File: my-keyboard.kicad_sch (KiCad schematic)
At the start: 156 parts, among them J1 AVR-ISP-6, SW1 SW_Push, U1 ATmega32U4-AU, Y1 16MHz

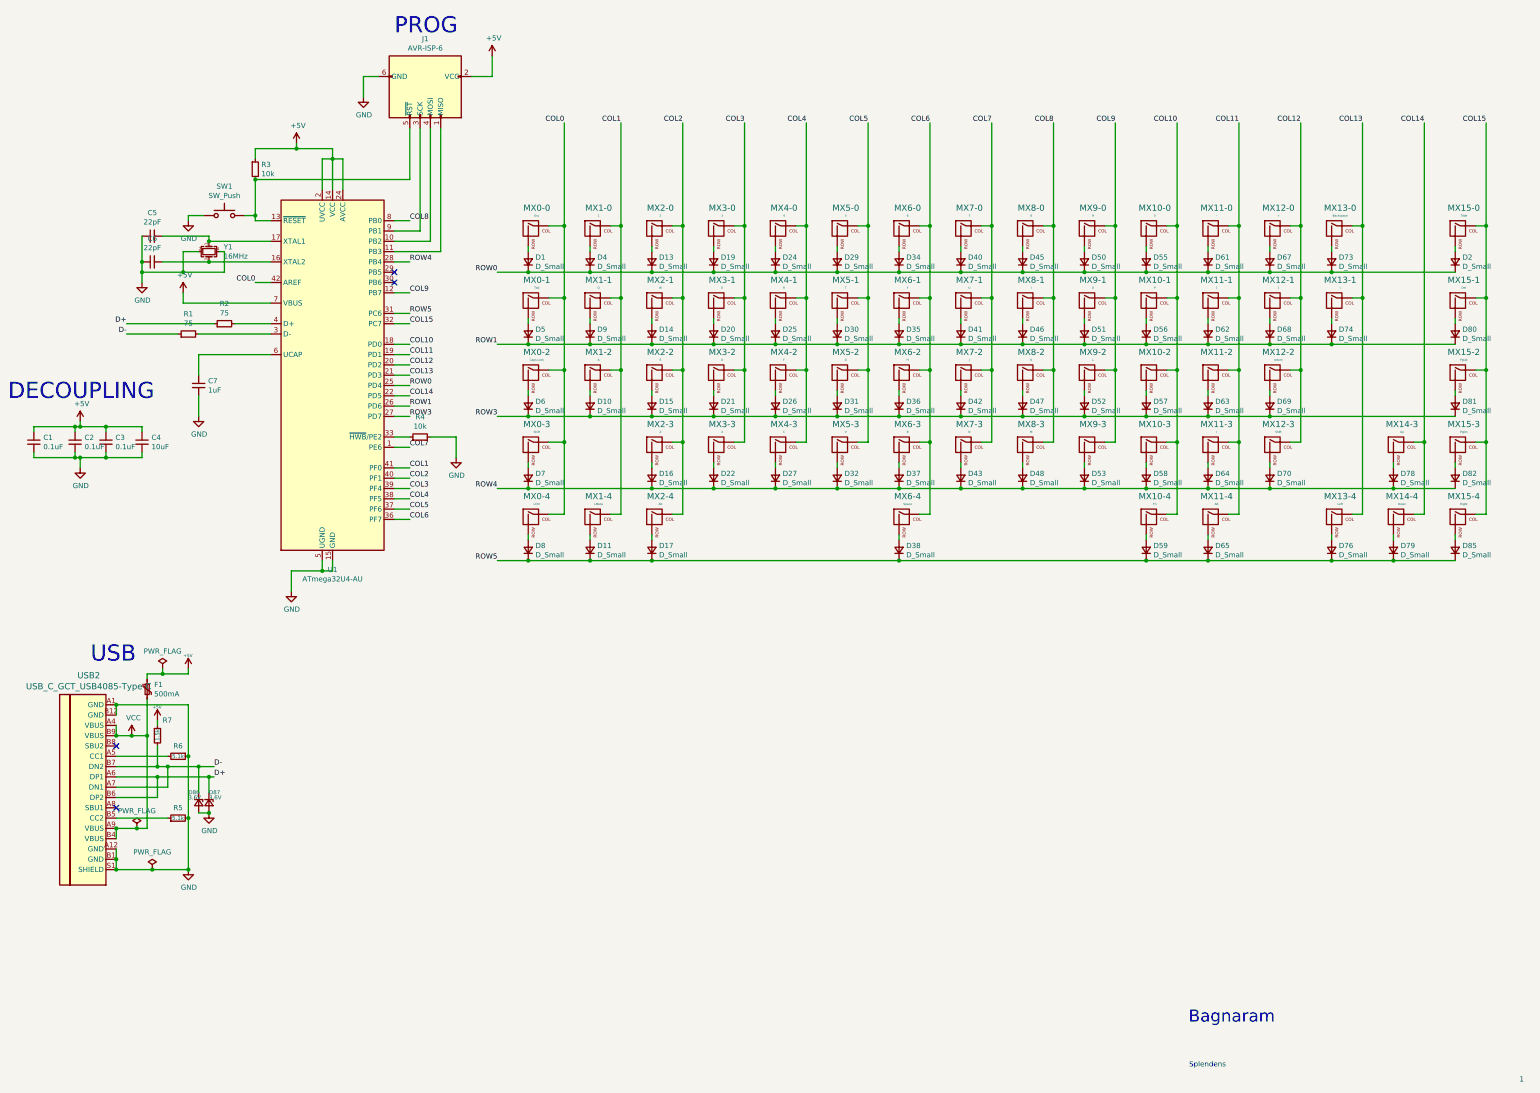
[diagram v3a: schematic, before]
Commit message: different usb footprint
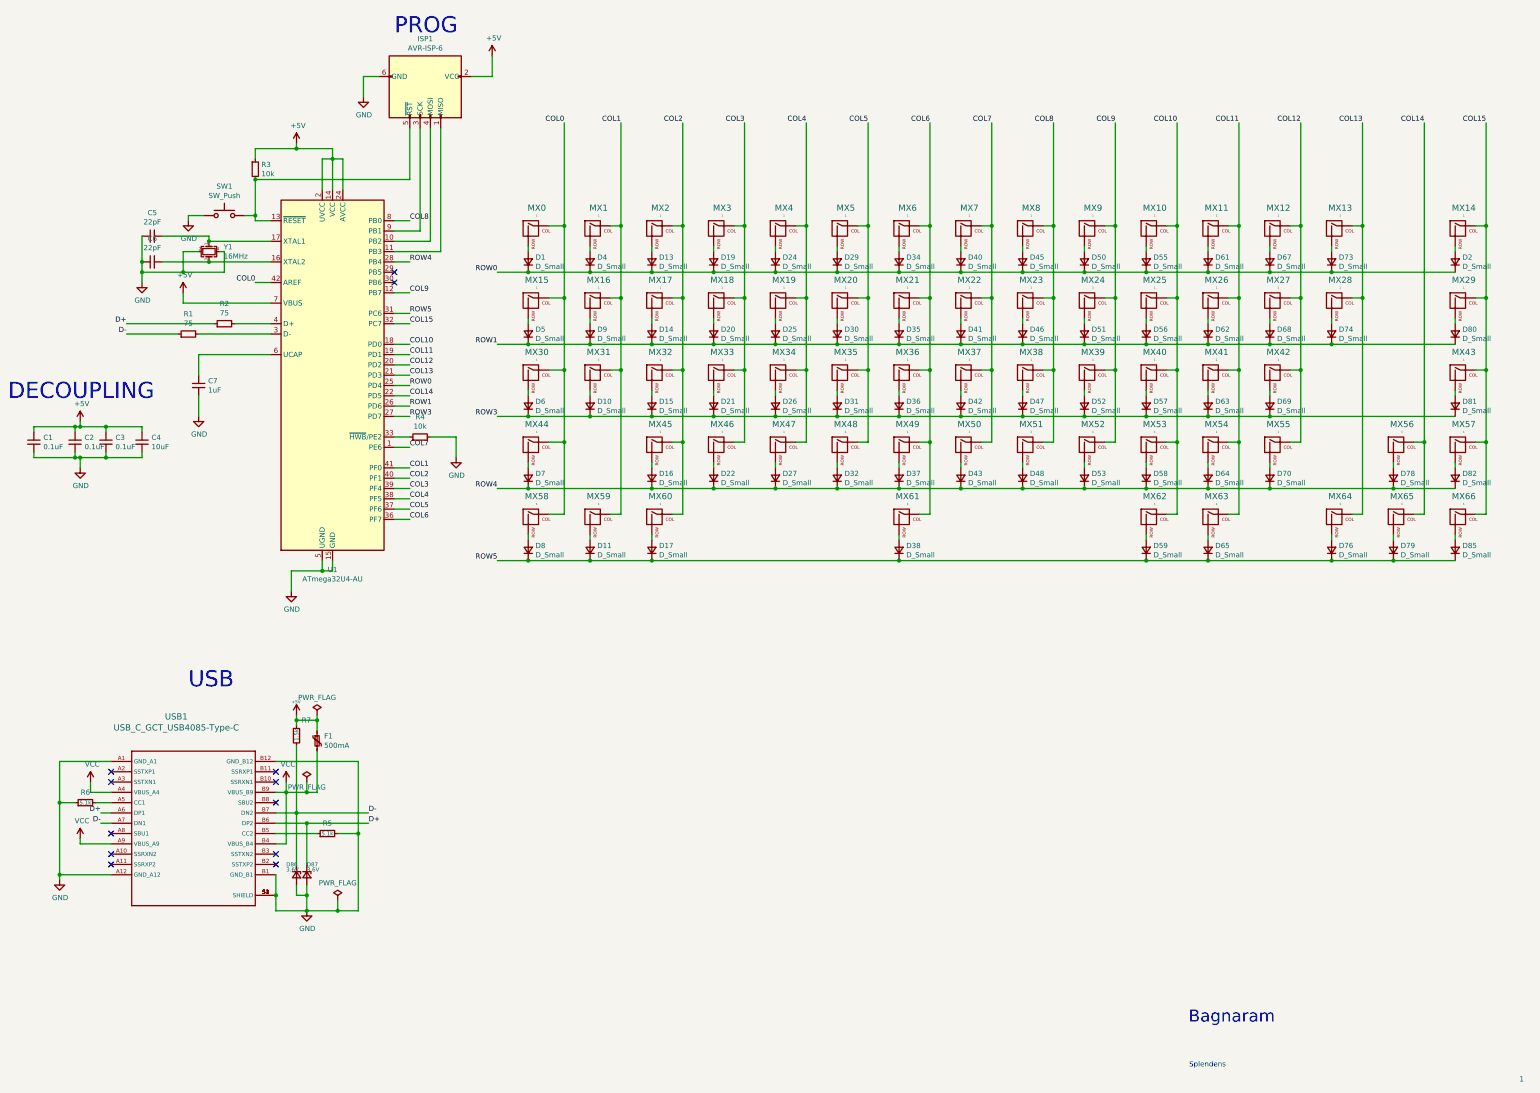
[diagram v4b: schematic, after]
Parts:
- C1, C2, C3: SKU (none) -> CC0805JPX7R8BB104
- C4: SKU (none) -> CGA4J1X7S1E106K125AC
- C5, C6: SKU (none) -> C0805X220K3GACAUTO
- C7: SKU (none) -> C0805C105M8RACAUTO
- D1, D10, D11, D13, D14, D15, D16, D17, D19, D2, D20, D21, D22, D24, D25, D26, D27, D29, D30, D31, D32, D34, D35, D36, D37, D38, D4, D40, D41, D42, D43, D45, D46, D47, D48, D5, D50, D51, D52, D53, D55, D56, D57, D58, D59, D6, D61, D62, D63, D64, D65, D67, D68, D69, D7, D70, D73, D74, D76, D78, D79, D8, D80, D81, D82, D85, D9: SKU (none) -> 1N4148W-E3-08
- D86, D87: SKU (none) -> MMSZ4685T1G
- F1: SKU (none) -> MF-R050
- ISP1: renamed from J1; SKU (none) -> 68602-406HLF
- MX0: renamed from MX0-0; value Esc -> 1; SKU (none) -> PCB Mount Gateron Switches (5 Legs) Brown
- MX1: renamed from MX1-0; SKU (none) -> PCB Mount Gateron Switches (5 Legs) Brown
- MX10: renamed from MX10-0; value 0 -> 1; SKU (none) -> PCB Mount Gateron Switches (5 Legs) Brown
- MX11: renamed from MX11-0; value - -> 1; SKU (none) -> PCB Mount Gateron Switches (5 Legs) Brown
- MX12: renamed from MX12-0; value = -> 1; SKU (none) -> PCB Mount Gateron Switches (5 Legs) Brown
- MX13: renamed from MX13-0; value Backspace -> 1; SKU (none) -> PCB Mount Gateron Switches (5 Legs) Brown
- MX14: renamed from MX15-0; value Tilde -> 1; SKU (none) -> PCB Mount Gateron Switches (5 Legs) Brown
- MX15: renamed from MX0-1; value Tab -> 1; SKU (none) -> PCB Mount Gateron Switches (5 Legs) Brown
- MX16: renamed from MX1-1; value Q -> 1; SKU (none) -> PCB Mount Gateron Switches (5 Legs) Brown
- MX17: renamed from MX2-1; value W -> 1; SKU (none) -> PCB Mount Gateron Switches (5 Legs) Brown
- MX18: renamed from MX3-1; value E -> 1; SKU (none) -> PCB Mount Gateron Switches (5 Legs) Brown
- MX19: renamed from MX4-1; value R -> 1; SKU (none) -> PCB Mount Gateron Switches (5 Legs) Brown
- MX2: renamed from MX2-0; value 2 -> 1; SKU (none) -> PCB Mount Gateron Switches (5 Legs) Brown
- MX20: renamed from MX5-1; value T -> 1; SKU (none) -> PCB Mount Gateron Switches (5 Legs) Brown
- MX21: renamed from MX6-1; value Y -> 1; SKU (none) -> PCB Mount Gateron Switches (5 Legs) Brown
- MX22: renamed from MX7-1; value U -> 1; SKU (none) -> PCB Mount Gateron Switches (5 Legs) Brown
- MX23: renamed from MX8-1; value I -> 1; SKU (none) -> PCB Mount Gateron Switches (5 Legs) Brown
- MX24: renamed from MX9-1; value O -> 1; SKU (none) -> PCB Mount Gateron Switches (5 Legs) Brown
- MX25: renamed from MX10-1; value P -> 1; SKU (none) -> PCB Mount Gateron Switches (5 Legs) Brown
- MX26: renamed from MX11-1; value [ -> 1; SKU (none) -> PCB Mount Gateron Switches (5 Legs) Brown
- MX27: renamed from MX12-1; value ] -> 1; SKU (none) -> PCB Mount Gateron Switches (5 Legs) Brown
- MX28: renamed from MX13-1; value \ -> 1; SKU (none) -> PCB Mount Gateron Switches (5 Legs) Brown
- MX29: renamed from MX15-1; value Del -> 1; SKU (none) -> PCB Mount Gateron Switches (5 Legs) Brown
- MX3: renamed from MX3-0; value 3 -> 1; SKU (none) -> PCB Mount Gateron Switches (5 Legs) Brown
- MX30: renamed from MX0-2; value Caps Lock -> 1; SKU (none) -> PCB Mount Gateron Switches (5 Legs) Brown
- MX31: renamed from MX1-2; value A -> 1; SKU (none) -> PCB Mount Gateron Switches (5 Legs) Brown
- MX32: renamed from MX2-2; value S -> 1; SKU (none) -> PCB Mount Gateron Switches (5 Legs) Brown
- MX33: renamed from MX3-2; value D -> 1; SKU (none) -> PCB Mount Gateron Switches (5 Legs) Brown
- MX34: renamed from MX4-2; value F -> 1; SKU (none) -> PCB Mount Gateron Switches (5 Legs) Brown
- MX35: renamed from MX5-2; value G -> 1; SKU (none) -> PCB Mount Gateron Switches (5 Legs) Brown
- MX36: renamed from MX6-2; value H -> 1; SKU (none) -> PCB Mount Gateron Switches (5 Legs) Brown
- MX37: renamed from MX7-2; value J -> 1; SKU (none) -> PCB Mount Gateron Switches (5 Legs) Brown
- MX38: renamed from MX8-2; value K -> 1; SKU (none) -> PCB Mount Gateron Switches (5 Legs) Brown
- MX39: renamed from MX9-2; value L -> 1; SKU (none) -> PCB Mount Gateron Switches (5 Legs) Brown
- MX4: renamed from MX4-0; value 4 -> 1; SKU (none) -> PCB Mount Gateron Switches (5 Legs) Brown
- MX40: renamed from MX10-2; value ; -> 1; SKU (none) -> PCB Mount Gateron Switches (5 Legs) Brown
- MX41: renamed from MX11-2; value ' -> 1; SKU (none) -> PCB Mount Gateron Switches (5 Legs) Brown
- MX42: renamed from MX12-2; value return -> 1; SKU (none) -> PCB Mount Gateron Switches (5 Legs) Brown
- MX43: renamed from MX15-2; value PgUp -> 1; SKU (none) -> PCB Mount Gateron Switches (5 Legs) Brown
- MX44: renamed from MX0-3; value Shift -> 1; SKU (none) -> PCB Mount Gateron Switches (5 Legs) Brown
- MX45: renamed from MX2-3; value Z -> 1; SKU (none) -> PCB Mount Gateron Switches (5 Legs) Brown
- MX46: renamed from MX3-3; value X -> 1; SKU (none) -> PCB Mount Gateron Switches (5 Legs) Brown
- MX47: renamed from MX4-3; value C -> 1; SKU (none) -> PCB Mount Gateron Switches (5 Legs) Brown
- MX48: renamed from MX5-3; value V -> 1; SKU (none) -> PCB Mount Gateron Switches (5 Legs) Brown
- MX49: renamed from MX6-3; value B -> 1; SKU (none) -> PCB Mount Gateron Switches (5 Legs) Brown
- MX5: renamed from MX5-0; value 5 -> 1; SKU (none) -> PCB Mount Gateron Switches (5 Legs) Brown
- MX50: renamed from MX7-3; value N -> 1; SKU (none) -> PCB Mount Gateron Switches (5 Legs) Brown
- MX51: renamed from MX8-3; value M -> 1; SKU (none) -> PCB Mount Gateron Switches (5 Legs) Brown
- MX52: renamed from MX9-3; value , -> 1; SKU (none) -> PCB Mount Gateron Switches (5 Legs) Brown
- MX53: renamed from MX10-3; value . -> 1; SKU (none) -> PCB Mount Gateron Switches (5 Legs) Brown
- MX54: renamed from MX11-3; value / -> 1; SKU (none) -> PCB Mount Gateron Switches (5 Legs) Brown
- MX55: renamed from MX12-3; value Shift -> 1; SKU (none) -> PCB Mount Gateron Switches (5 Legs) Brown
- MX56: renamed from MX14-3; value Up -> 1; SKU (none) -> PCB Mount Gateron Switches (5 Legs) Brown
- MX57: renamed from MX15-3; value PgDn -> 1; SKU (none) -> PCB Mount Gateron Switches (5 Legs) Brown
- MX58: renamed from MX0-4; value LCtrl -> 1; SKU (none) -> PCB Mount Gateron Switches (5 Legs) Brown
- MX59: renamed from MX1-4; value LMeta -> 1; SKU (none) -> PCB Mount Gateron Switches (5 Legs) Brown
- MX6: renamed from MX6-0; value 6 -> 1; SKU (none) -> PCB Mount Gateron Switches (5 Legs) Brown
- MX60: renamed from MX2-4; value Alt -> 1; SKU (none) -> PCB Mount Gateron Switches (5 Legs) Brown
- MX61: renamed from MX6-4; value Space -> 1; SKU (none) -> PCB Mount Gateron Switches (5 Legs) Brown
- MX62: renamed from MX10-4; value Fn -> 1; SKU (none) -> PCB Mount Gateron Switches (5 Legs) Brown
- MX63: renamed from MX11-4; value Alt -> 1; SKU (none) -> PCB Mount Gateron Switches (5 Legs) Brown
- MX64: renamed from MX13-4; value Left -> 1; SKU (none) -> PCB Mount Gateron Switches (5 Legs) Brown
- MX65: renamed from MX14-4; value Down -> 1; SKU (none) -> PCB Mount Gateron Switches (5 Legs) Brown
- MX66: renamed from MX15-4; value Right -> 1; SKU (none) -> PCB Mount Gateron Switches (5 Legs) Brown
- MX7: renamed from MX7-0; value 7 -> 1; SKU (none) -> PCB Mount Gateron Switches (5 Legs) Brown
- MX8: renamed from MX8-0; value 8 -> 1; SKU (none) -> PCB Mount Gateron Switches (5 Legs) Brown
- MX9: renamed from MX9-0; value 9 -> 1; SKU (none) -> PCB Mount Gateron Switches (5 Legs) Brown
- R1, R2: SKU (none) -> GWCR0805-75RFT5
- R3, R4: SKU (none) -> WCR0805-10KFI
- R5, R6: SKU (none) -> CR0805-FX-5101ELF
- R7: SKU (none) -> CR0805-FX-1501ELF
- SW1: footprint Random Keyboard Parts:SKQG-1155865 -> Random Keyboard Parts:SKQGADE010; SKU (none) -> SKQGADE010
- U1: SKU (none) -> ATmega32U4-AU
- USB1: renamed from USB2; symbol discipline-pcb-rescue:USB_C_GCT_USB4085-Type-C -> 10137061-00021LF:10137061-00021LF; SKU (none) -> 10137061-00021LF
- Y1: SKU (none) -> NX3225GA-16.000M-STD-CRG-2
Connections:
- net GND: now also USB1.S2 (SHIELD), USB1.S3 (SHIELD), USB1.S4 (SHIELD)
- no-connect marks 4 -> 12
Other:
- moved on the sheet: D86, D87, F1, R5, R6, R7

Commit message: Generated gerbers
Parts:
- removed USB1: USB_C_GCT_USB4085-Type-C, cftkb:USB_C_GCT_USB4085, symbol 10137061-00021LF:10137061-00021LF
- added USB1: Wurth-632723300011, Type-C:Wurth-632723300011, symbol Type-C:Wurth-632723300011
- C1, C2, C3: value 0.1uF -> 0.1u
- C4: value 10uF -> 10u
- C5, C6: value 22pF -> 22p
- C7: value 1uF -> 1u
- R1, R2: value 75 -> 22
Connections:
- net D+: now also USB1.18 (Dp2), USB1.6 (Dp1)
- net D-: now also USB1.19 (Dn2), USB1.7 (Dn1)
- net GND: now also USB1.1 (GND), USB1.12 (GND), USB1.13 (GND), USB1.24 (GND), USB1.25 (Center_Plate_Pin), USB1.26 (Connector_Legs), USB1.27 (Under-Barrel_Pads)
- net VCC: now also USB1.16 (VBUS), USB1.21 (VBUS), USB1.4 (VBUS), USB1.9 (VBUS)
- net at R5.1: now also USB1.17 (CC2)
- net at R6.2: now also USB1.5 (CC1)
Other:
- moved on the sheet: C5, C6, D86, D87, F1, R5, R6, R7, SW1
